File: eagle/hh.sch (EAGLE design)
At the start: 7 parts

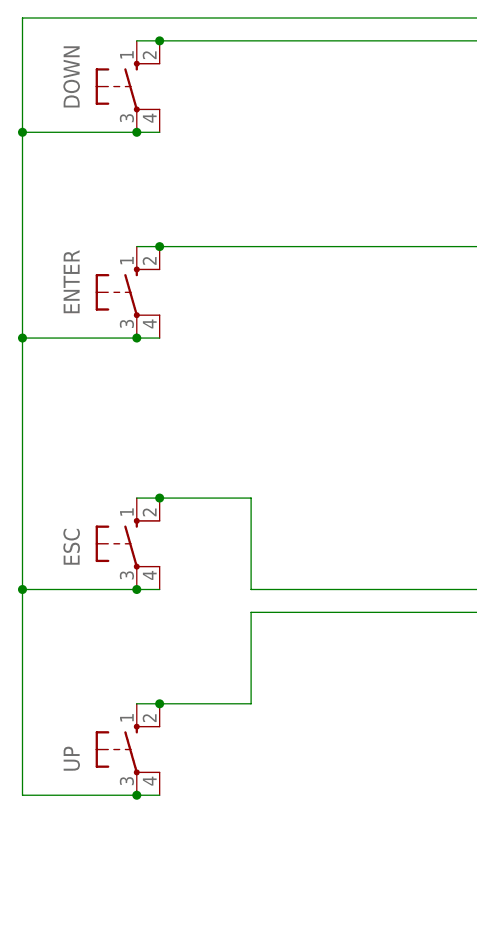
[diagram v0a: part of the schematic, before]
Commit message: silkscreen edits
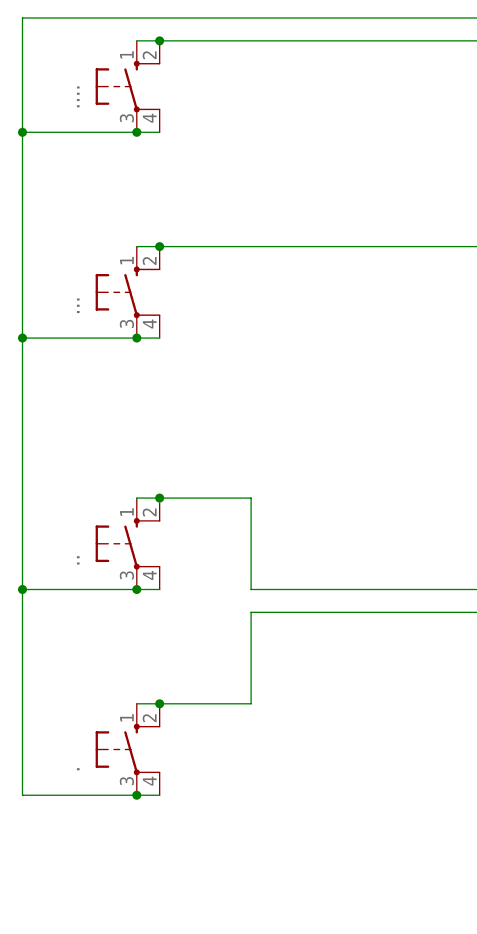
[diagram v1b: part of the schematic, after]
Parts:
- renumbered DOWN to ...., ENTER to ..., ESC to .., UP to .
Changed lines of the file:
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@@
 </classes>
 <parts>
-<part name="DOWN" library="switch-omron" deviceset="10-XX" device=""/>
-<part name="ENTER" library="switch-omron" deviceset="10-XX" device=""/>
-<part name="ESC" library="switch-omron" deviceset="10-XX" device=""/>
-<part name="UP" library="switch-omron" deviceset="10-XX" device=""/>
+<part name="...." library="switch-omron" deviceset="10-XX" device=""/>
+<part name="..." library="switch-omron" deviceset="10-XX" device=""/>
+<part name=".." library="switch-omron" deviceset="10-XX" device=""/>
+<part name="." library="switch-omron" deviceset="10-XX" device=""/>
 <part name="ESP12E_DEVKIT" library="ESP12E_DEVKIT" deviceset="ESP12E_DEVKIT" device=""/>
 <part name="FRAME1" library="frames" deviceset="FRAME_A_L" device=""/>
@@
 </plain>
 <instances>
-<instance part="DOWN" gate="1" x="22.86" y="142.24"/>
-<instance part="ENTER" gate="1" x="22.86" y="119.38"/>
-<instance part="ESC" gate="1" x="22.86" y="91.44"/>
-<instance part="UP" gate="1" x="22.86" y="68.58"/>
+<instance part="...." gate="1" x="22.86" y="142.24"/>
+<instance part="..." gate="1" x="22.86" y="119.38"/>
+<instance part=".." gate="1" x="22.86" y="91.44"/>
+<instance part="." gate="1" x="22.86" y="68.58"/>
 <instance part="ESP12E_DEVKIT" gate="G$1" x="119.38" y="93.98" rot="R180"/>
 <instance part="FRAME1" gate="G$1" x="-22.86" y="-12.7"/>
@@
 <segment>
 <pinref part="ESP12E_DEVKIT" gate="G$1" pin="D3"/>
-<pinref part="UP" gate="1" pin="S1"/>
+<pinref part="." gate="1" pin="S1"/>
 <wire x1="101.6" y1="83.82" x2="35.56" y2="83.82" width="0.1524" layer="91"/>
 <wire x1="35.56" y1="83.82" x2="35.56" y2="73.66" width="0.1524" layer="91"/>
 <wire x1="35.56" y1="73.66" x2="25.4" y2="73.66" width="0.1524" layer="91"/>
-<pinref part="UP" gate="1" pin="S"/>
+<pinref part="." gate="1" pin="S"/>
 <wire x1="22.86" y1="73.66" x2="25.4" y2="73.66" width="0.1524" layer="91"/>
 <junction x="25.4" y="73.66"/>
@@
 <segment>
 <pinref part="ESP12E_DEVKIT" gate="G$1" pin="D4"/>
-<pinref part="ESC" gate="1" pin="S1"/>
+<pinref part=".." gate="1" pin="S1"/>
 <wire x1="101.6" y1="86.36" x2="35.56" y2="86.36" width="0.1524" layer="91"/>
 <wire x1="35.56" y1="86.36" x2="35.56" y2="96.52" width="0.1524" layer="91"/>
 <wire x1="35.56" y1="96.52" x2="25.4" y2="96.52" width="0.1524" layer="91"/>
-<pinref part="ESC" gate="1" pin="S"/>
+<pinref part=".." gate="1" pin="S"/>
 <wire x1="22.86" y1="96.52" x2="25.4" y2="96.52" width="0.1524" layer="91"/>
 <junction x="25.4" y="96.52"/>
@@
 <net name="N$8" class="0">
 <segment>
-<pinref part="ENTER" gate="1" pin="S1"/>
+<pinref part="..." gate="1" pin="S1"/>
 <wire x1="60.96" y1="124.46" x2="25.4" y2="124.46" width="0.1524" layer="91"/>
-<pinref part="ENTER" gate="1" pin="S"/>
+<pinref part="..." gate="1" pin="S"/>
 <wire x1="22.86" y1="124.46" x2="25.4" y2="124.46" width="0.1524" layer="91"/>
 <junction x="25.4" y="124.46"/>
@@
 <net name="N$9" class="0">
 <segment>
-<pinref part="DOWN" gate="1" pin="S1"/>
+<pinref part="...." gate="1" pin="S1"/>
 <wire x1="63.5" y1="147.32" x2="25.4" y2="147.32" width="0.1524" layer="91"/>
-<pinref part="DOWN" gate="1" pin="S"/>
+<pinref part="...." gate="1" pin="S"/>
 <wire x1="22.86" y1="147.32" x2="25.4" y2="147.32" width="0.1524" layer="91"/>
 <junction x="25.4" y="147.32"/>
@@
 <wire x1="66.04" y1="109.22" x2="66.04" y2="149.86" width="0.1524" layer="91"/>
 <junction x="101.6" y="109.22"/>
-<pinref part="UP" gate="1" pin="P"/>
+<pinref part="." gate="1" pin="P"/>
 <wire x1="22.86" y1="63.5" x2="10.16" y2="63.5" width="0.1524" layer="91"/>
 <wire x1="10.16" y1="63.5" x2="10.16" y2="86.36" width="0.1524" layer="91"/>
 <wire x1="10.16" y1="86.36" x2="10.16" y2="114.3" width="0.1524" layer="91"/>
 <wire x1="10.16" y1="114.3" x2="10.16" y2="137.16" width="0.1524" layer="91"/>
-<pinref part="ESC" gate="1" pin="P"/>
+<pinref part=".." gate="1" pin="P"/>
 <wire x1="22.86" y1="86.36" x2="10.16" y2="86.36" width="0.1524" layer="91"/>
 <junction x="10.16" y="86.36"/>
-<pinref part="ENTER" gate="1" pin="P"/>
+<pinref part="..." gate="1" pin="P"/>
 <wire x1="22.86" y1="114.3" x2="10.16" y2="114.3" width="0.1524" layer="91"/>
 <junction x="10.16" y="114.3"/>
-<pinref part="DOWN" gate="1" pin="P"/>
+<pinref part="...." gate="1" pin="P"/>
 <wire x1="22.86" y1="137.16" x2="10.16" y2="137.16" width="0.1524" layer="91"/>
-<pinref part="DOWN" gate="1" pin="P1"/>
+<pinref part="...." gate="1" pin="P1"/>
 <wire x1="25.4" y1="137.16" x2="22.86" y2="137.16" width="0.1524" layer="91"/>
 <junction x="22.86" y="137.16"/>
-<pinref part="ENTER" gate="1" pin="P1"/>
+<pinref part="..." gate="1" pin="P1"/>
 <wire x1="25.4" y1="114.3" x2="22.86" y2="114.3" width="0.1524" layer="91"/>
 <junction x="22.86" y="114.3"/>
-<pinref part="ESC" gate="1" pin="P1"/>
+<pinref part=".." gate="1" pin="P1"/>
 <wire x1="25.4" y1="86.36" x2="22.86" y2="86.36" width="0.1524" layer="91"/>
 <junction x="22.86" y="86.36"/>
-<pinref part="UP" gate="1" pin="P1"/>
+<pinref part="." gate="1" pin="P1"/>
 <wire x1="25.4" y1="63.5" x2="22.86" y2="63.5" width="0.1524" layer="91"/>
 <junction x="22.86" y="63.5"/>

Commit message: cleanup first release
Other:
- note added: "DE:AD:10:C5"
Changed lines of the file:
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@@
 <?xml version="1.0" encoding="utf-8"?>
 <!DOCTYPE eagle SYSTEM "eagle.dtd">
-<eagle version="7.5.0">
+<eagle version="8.7.1">
 <drawing>
 <settings>
 <setting alwaysvectorfont="no"/>
+<setting keepoldvectorfont="yes"/>
 <setting verticaltext="up"/>
 </settings>
@@
 <description>hackharder</description>
 <plain>
+<text x="154.94" y="15.24" size="5.08" layer="91">DE:AD:10:C5</text>
 </plain>
 <instances>
